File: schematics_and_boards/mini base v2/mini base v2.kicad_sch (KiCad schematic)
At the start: 31 parts, among them J1 Micro Bypass Header, J2 Debug Header, J3 Ext Pwr, U1 BC840, U2 LSM6DSOXTR, U3 OPT4001DTSR, U4 OPT4001DTSR, Y1 32.768KHz

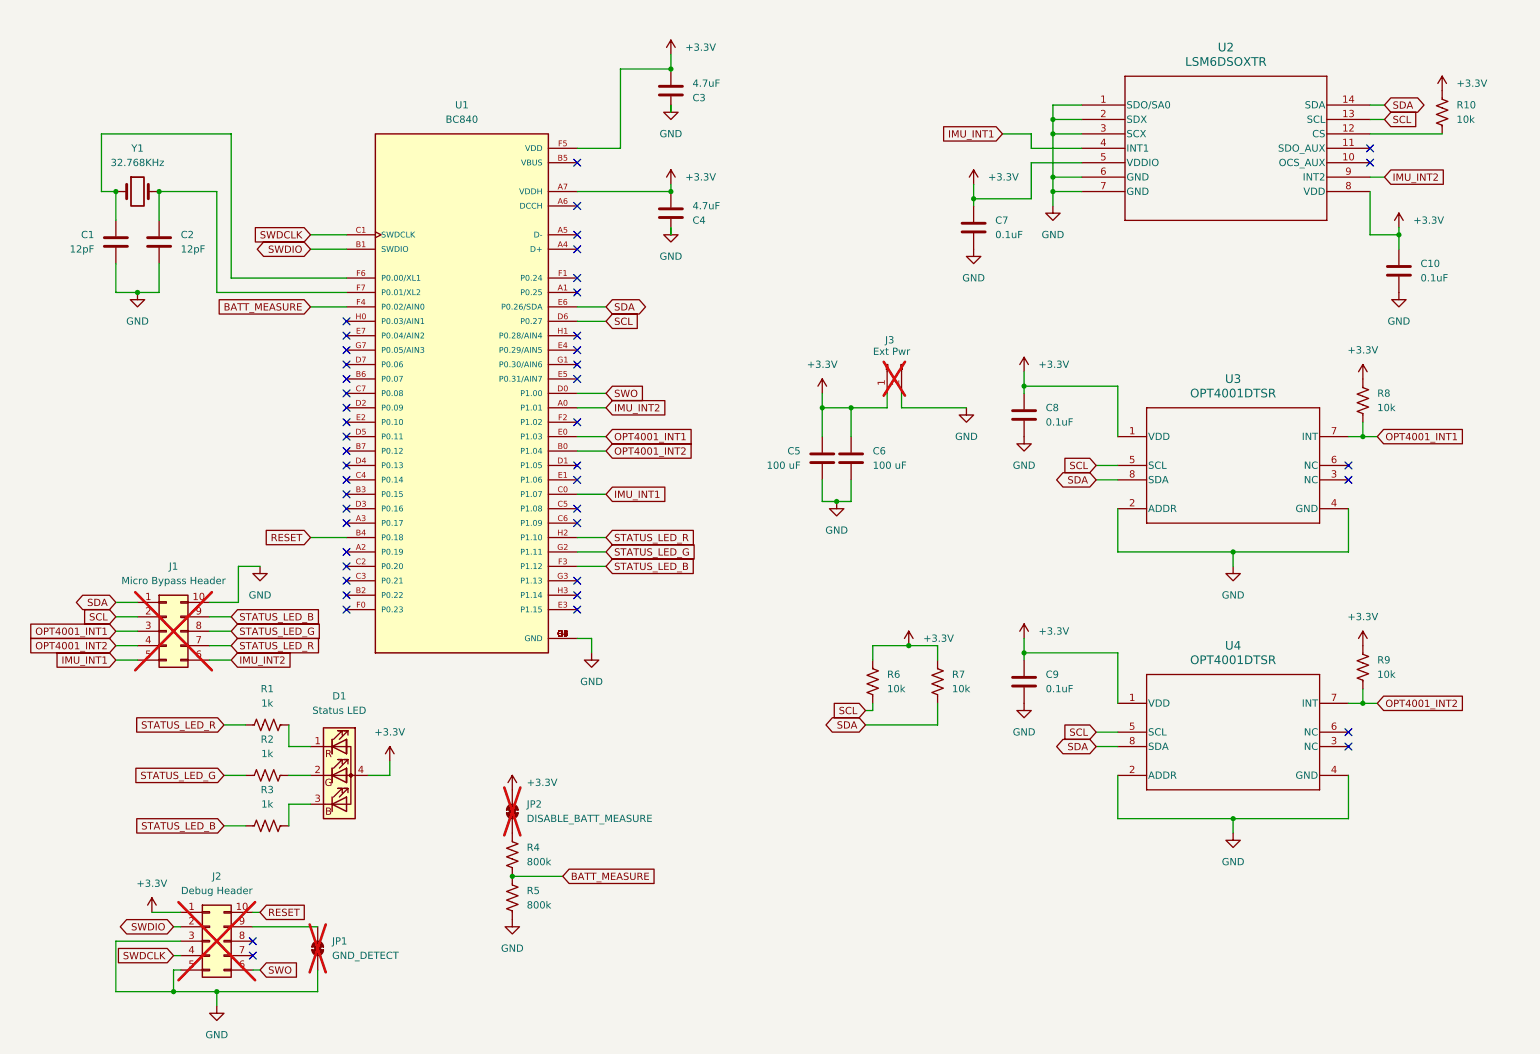
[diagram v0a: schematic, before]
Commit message: pcb v1 sent for manufacture
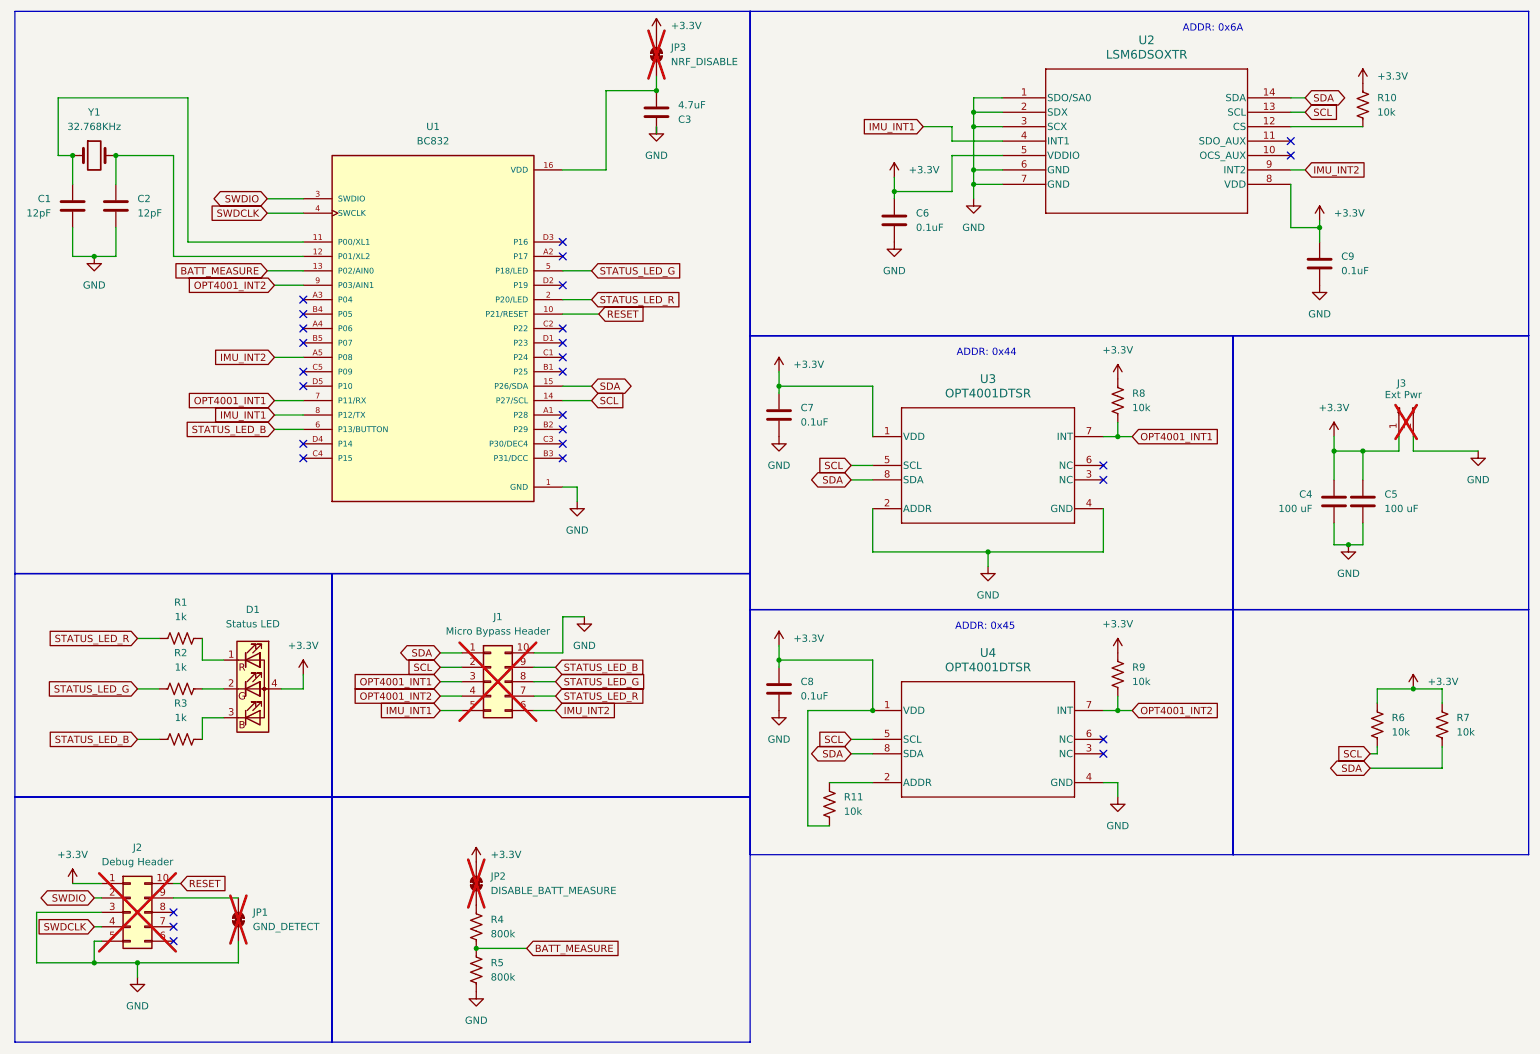
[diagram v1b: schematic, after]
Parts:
- removed C4: 4.7uF, Capacitor_SMD:C_0603_1608Metric, symbol Device:C
- removed U1: BC840, anichno:MODULE_BC840, symbol anichno:BC840
- added JP3: NRF_DISABLE, Jumper:SolderJumper-2_P1.3mm_Bridged_RoundedPad1.0x1.5mm, symbol Jumper:SolderJumper_2_Bridged
- added R11: 10k, Resistor_SMD:R_0603_1608Metric, symbol Device:R_US
- added U1: BC832, anichno:BC832, symbol anichno:BC832
- J1: footprint Connector_PinHeader_1.27mm:PinHeader_2x05_P1.27mm_Vertical_SMD -> Connector_PinHeader_2.54mm:PinHeader_2x05_P2.54mm_Vertical_SMD
- renumbered C5 to C4, C6 to C5, C7 to C6, C8 to C7, C9 to C8, C10 to C9
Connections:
- net +3.3V: now also JP3.2 (B), R11.1; no longer C3.1
- net BATT_MEASURE: now also U1.13 (P02/AIN0)
- net GND: now also U1.1 (GND); no longer U4.2 (ADDR)
- net IMU_INT1: now also U1.8 (P12/TX)
- net IMU_INT2: now also U1.A5 (P08)
- net OPT4001_INT1: now also U1.7 (P11/RX)
- net OPT4001_INT2: now also U1.9 (P03/AIN1)
- net RESET: now also U1.10 (P21/RESET)
- net SCL: now also U1.14 (P27/SCL)
- net SDA: now also U1.15 (P26/SDA)
- net STATUS_LED_B: now also U1.6 (P13/BUTTON)
- net STATUS_LED_G: now also U1.5 (P18/LED)
- net STATUS_LED_R: now also U1.2 (P20/LED)
- net SWDCLK: now also U1.4 (SWCLK)
- net SWDIO: now also U1.3 (SWDIO)
- net at C1.2, Y1.1: now also U1.11 (P00/XL1)
- net at C2.2, Y1.2: now also U1.12 (P01/XL2)
- net SWO: no longer names the net of J2.6 (Pin_6)
- new net: C3.1, JP3.1 (A), U1.16 (VDD)
- new net: R11.2, U4.2 (ADDR)
- no-connect marks 46 -> 28
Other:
- note added: "ADDR: 0x44"
- note added: "ADDR: 0x45"
- note added: "ADDR: 0x6A"
- moved on the sheet: C1, C2, C3, C4, C5, C6, C7, C8, C9, D1, J1, J2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
